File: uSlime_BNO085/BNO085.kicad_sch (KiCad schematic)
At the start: 12 parts, among them CN1 X1502WR-05K-N0SN, U5 BNO085

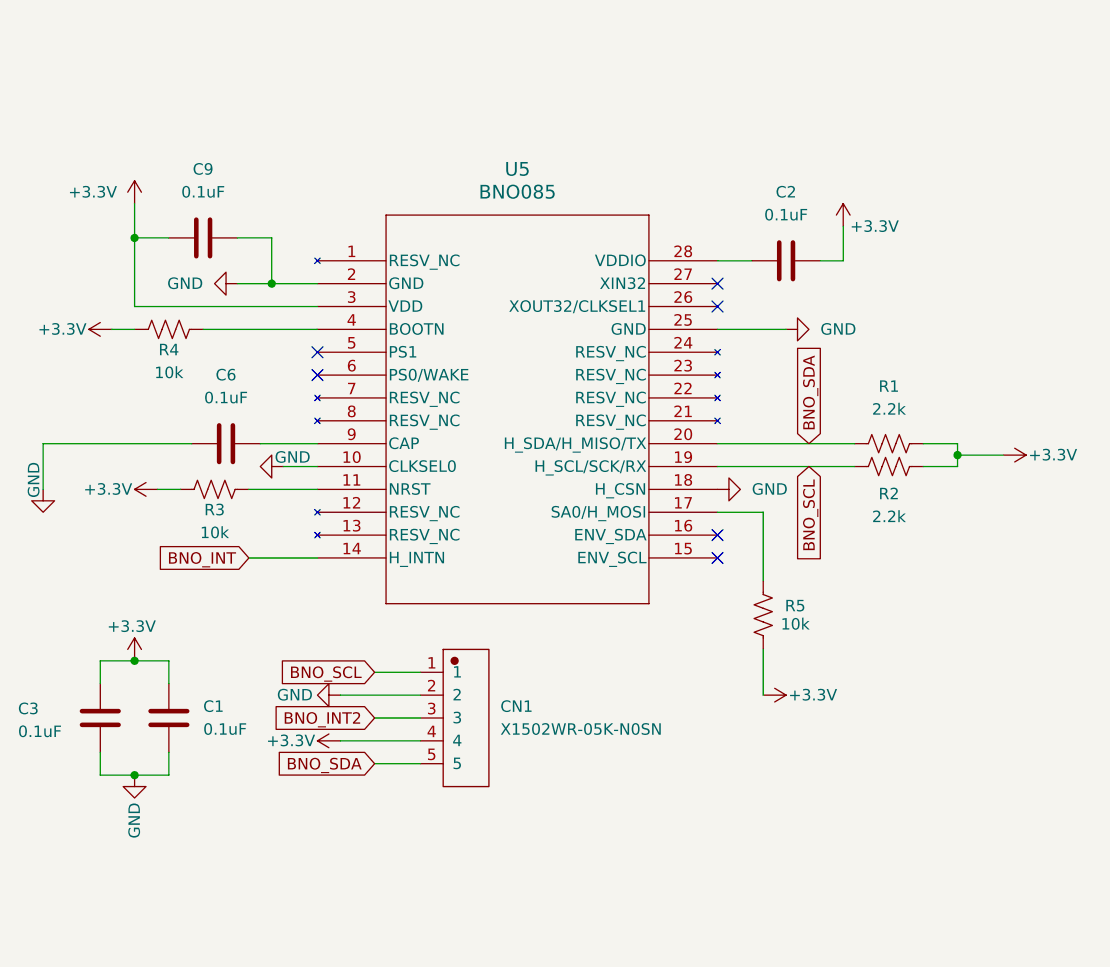
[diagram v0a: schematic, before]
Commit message: Faulty BNO085 footprint
First, I do not like you UltraLibrarian anymore, for you have wasted a
lot of time and effort (and money) on footprints that are just straight
up wrong. I am this close to unleashing unbridled rage on this but will
bottle it up for now.

Second, I took the BNO085 footprint from the official SlimeVR tracker
and put it in this project. At least they have the right footprint...

Stencils for the main microcontroller does not need to change but the
extension module got a revamp in favor of being more versatile. You can
now choose which I2C address the sensor operates on; just make sure you
bridge the right contacts.
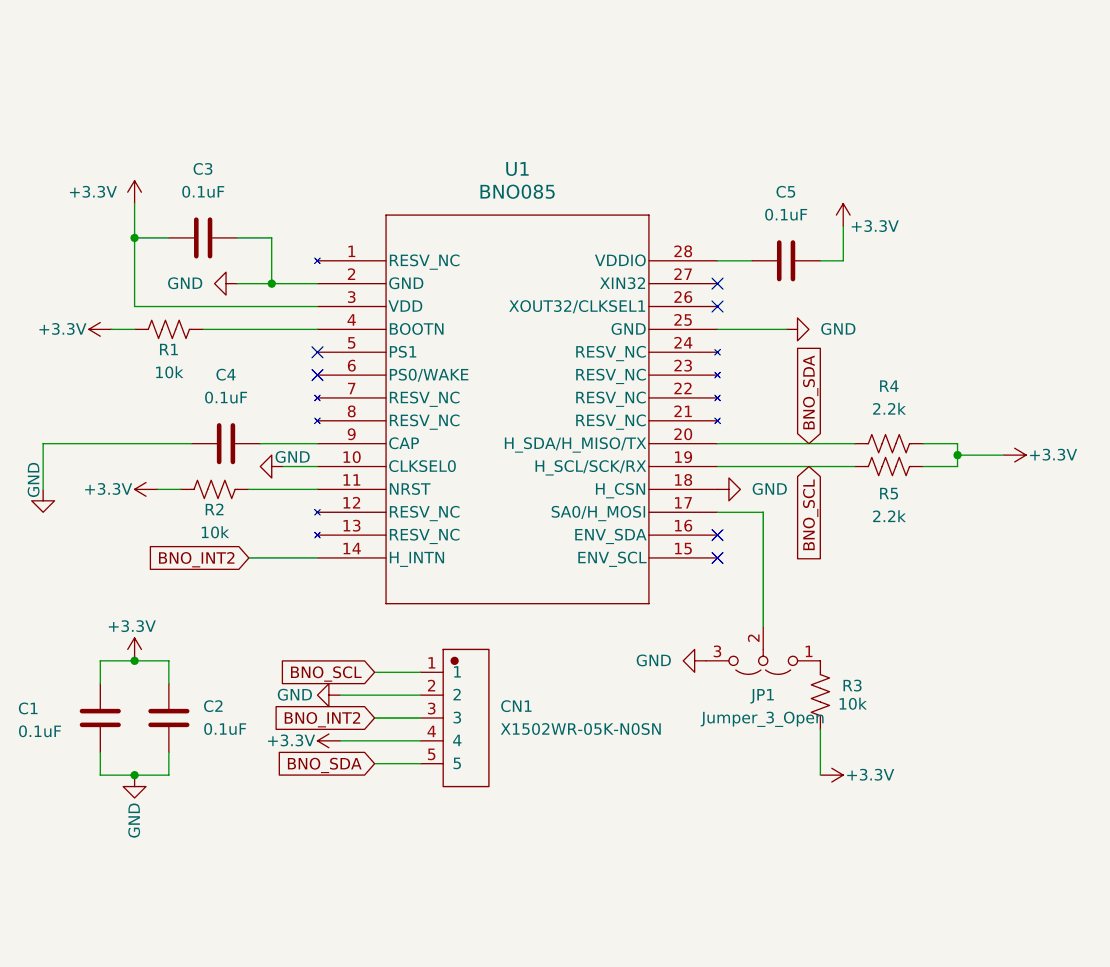
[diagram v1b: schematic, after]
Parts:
- removed R5: 10k, Resistor_SMD:R_0402_1005Metric, symbol uSlime:R_US
- added JP1: Jumper_3_Open, Jumper:SolderJumper-3_P1.3mm_Open_RoundedPad1.0x1.5mm, symbol uSlime:Jumper_3_Open
- added R3: 10k, Resistor_SMD:R_0402_1005Metric, symbol uSlime:R_US
- U1: renamed from U5; footprint uSlime-libs:LGA28_5.2X3.8_CEV -> uSlime-libs:BNO080
- renumbered C3 to C1, C1 to C2, C9 to C3, C6 to C4, C2 to C5, R4 to R1, R3 to R2, R1 to R4, R2 to R5
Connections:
- net BNO_INT is gone; now on net BNO_INT2: U1.14 (H_INTN)
- net +3.3V: now also R3.1
- net GND: now also JP1.3 (B)
- net at U1.17 (SA0/H_MOSI): now also JP1.2 (C)
- new net: JP1.1 (A), R3.2

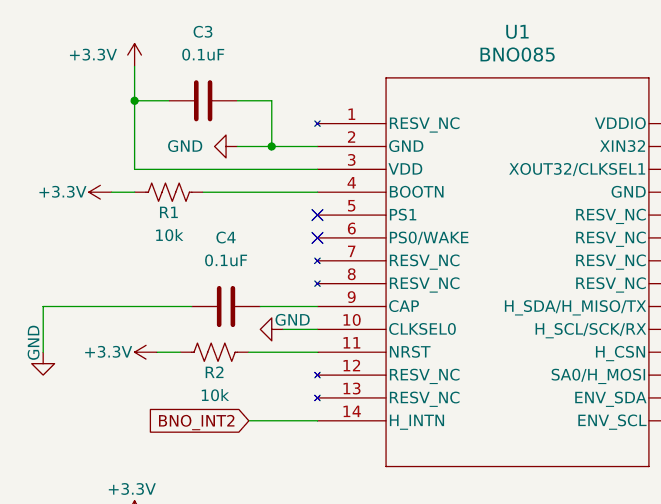
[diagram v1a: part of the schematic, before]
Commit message: update schmetic
fix pull up
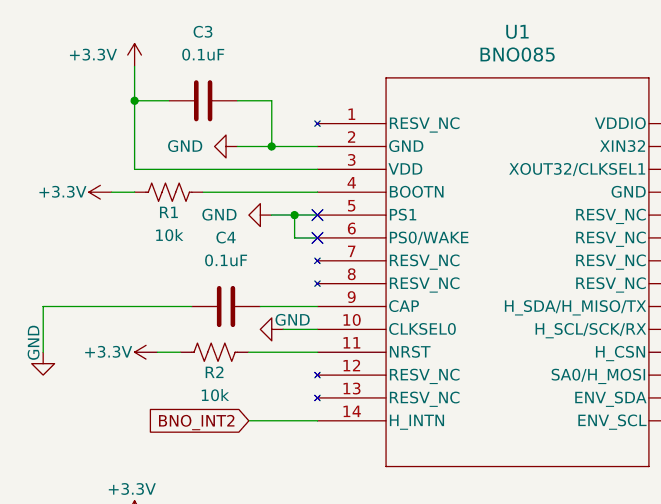
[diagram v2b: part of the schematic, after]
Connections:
- net GND: now also U1.5 (PS1), U1.6 (PS0/WAKE)
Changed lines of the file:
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@@
+	)
+	(junction
+		(at 113.03 87.63)
+		(diameter 0)
+		(color 0 0 0 0)
 	)
 	(junction
@@
 	(wire
 		(pts
+			(xy 113.03 90.17) (xy 115.57 90.17)
+		)
+		(stroke
+			(width 0)
+			(type default)
+		)
+	)
+	(wire
+		(pts
+			(xy 113.03 87.63) (xy 113.03 90.17)
+		)
+		(stroke
+			(width 0)
+			(type default)
+		)
+	)
+	(wire
+		(pts
 			(xy 110.49 74.93) (xy 110.49 80.01)
 		)
@@
 		(pts
 			(xy 163.83 77.47) (xy 160.02 77.47)
+		)
+		(stroke
+			(width 0)
+			(type default)
+		)
+	)
+	(wire
+		(pts
+			(xy 110.49 87.63) (xy 113.03 87.63)
+		)
+		(stroke
+			(width 0)
+			(type default)
+		)
+	)
+	(wire
+		(pts
+			(xy 113.03 87.63) (xy 115.57 87.63)
 		)
 		(stroke
@@
 					(unit 1)
 				)
+			)
+		)
+	)
+	(symbol
+		(lib_id "power:GND")
+		(at 110.49 87.63 270)
+		(unit 1)
+		(exclude_from_sim no)
+		(in_bom yes)
+		(on_board yes)
+		(dnp no)
+		(fields_autoplaced yes)
+		(property "Reference" "#PWR017"
+			(at 104.14 87.63 0)
+			(effects
+				(font
+					(size 1.27 1.27)
+				)
+				(hide yes)
+			)
+		)
+		(property "Value" "GND"
+			(at 106.68 87.6299 90)
+			(effects
+				(font
+					(size 1.27 1.27)
+				)
+				(justify right)
+			)
+		)
+		(property "Footprint" ""
+			(at 110.49 87.63 0)
+			(effects
+				(font
+					(size 1.27 1.27)
+				)
+				(hide yes)
+			)
+		)
+		(property "Datasheet" ""
+			(at 110.49 87.63 0)
+			(effects
+				(font
+					(size 1.27 1.27)
+				)
+				(hide yes)
+			)
+		)
+		(property "Description" "Power symbol creates a global label with name \"GND\" , ground"
+			(at 110.49 87.63 0)
+			(effects
+				(font
+					(size 1.27 1.27)
+				)
+				(hide yes)
+			)
+		)
+		(pin "1"
+		)
+		(instances
+			(project "uSlime_BNO085"
+				(path "/f32c1c49-f803-4e7c-a530-6db148a7ba36/1072de81-ddaf-4115-9b1e-8b480e2a0117"
+					(reference "#PWR017")
+					(unit 1)
+				)

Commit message: Update main PCB schematic
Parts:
- removed C5: 0.1uF, Capacitor_SMD:C_0402_1005Metric, symbol uSlime:C
- removed JP1: Jumper_3_Open, Jumper:SolderJumper-3_P1.3mm_Open_RoundedPad1.0x1.5mm, symbol uSlime:Jumper_3_Open
- removed R5: 2.2k, Resistor_SMD:R_0402_1005Metric, symbol uSlime:R_US
- R3: value 10k -> 2.2k
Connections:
- net +3.3V: now also CN1.2, R2.2, R4.1, U1.28 (VDDIO); no longer CN1.4, R2.1, R4.2
- net BNO_INT2: no longer U1.14 (H_INTN)
- net BNO_SCL: now also CN1.5, R4.2; no longer CN1.1
- net BNO_SDA: now also CN1.1, R3.2; no longer CN1.5, R4.1
- net GND: now also CN1.4; no longer CN1.2
- net at U1.11 (NRST): now also R2.1; no longer R2.2
- new net BNO_INT: U1.14 (H_INTN)
- no-connect marks 6 -> 5
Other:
- moved on the sheet: C1, C2

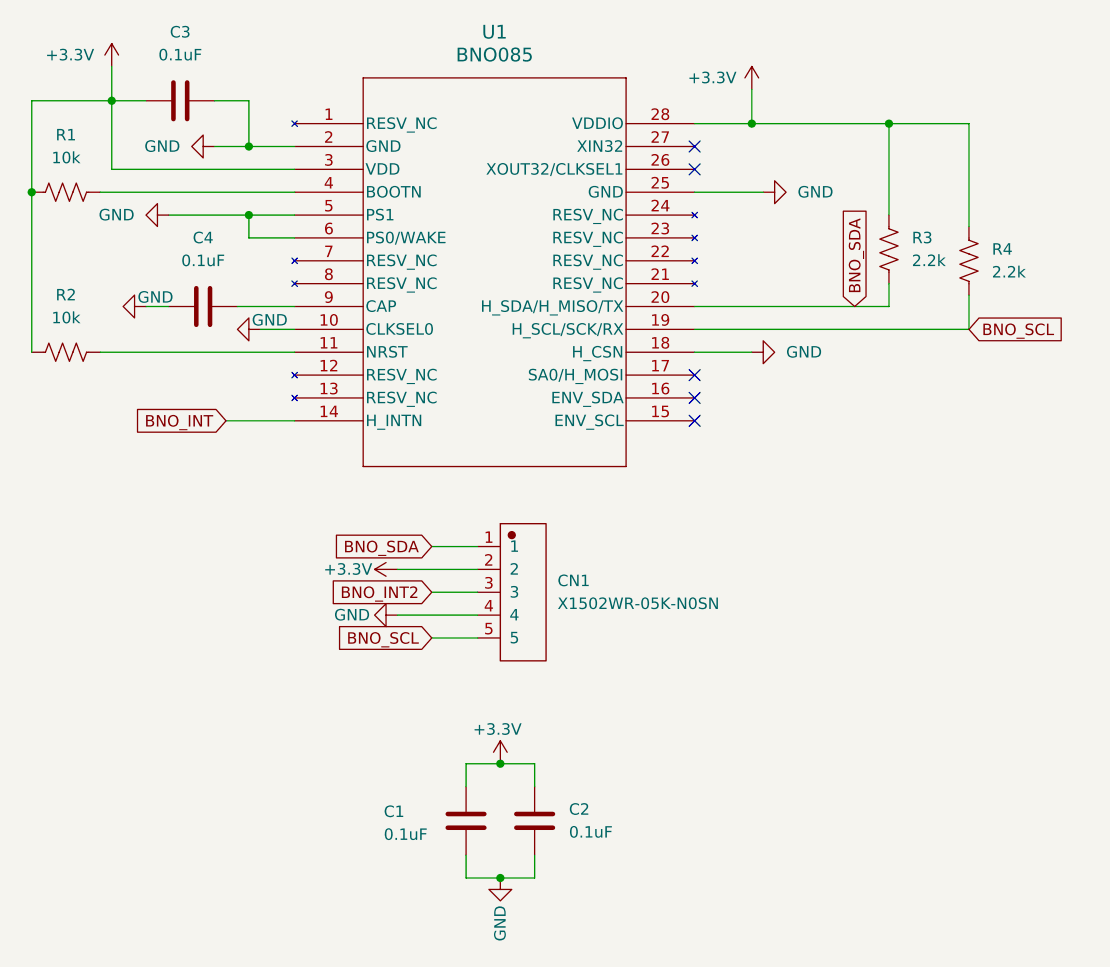
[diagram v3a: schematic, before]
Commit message: v0.0.2a Modify BNO I2C
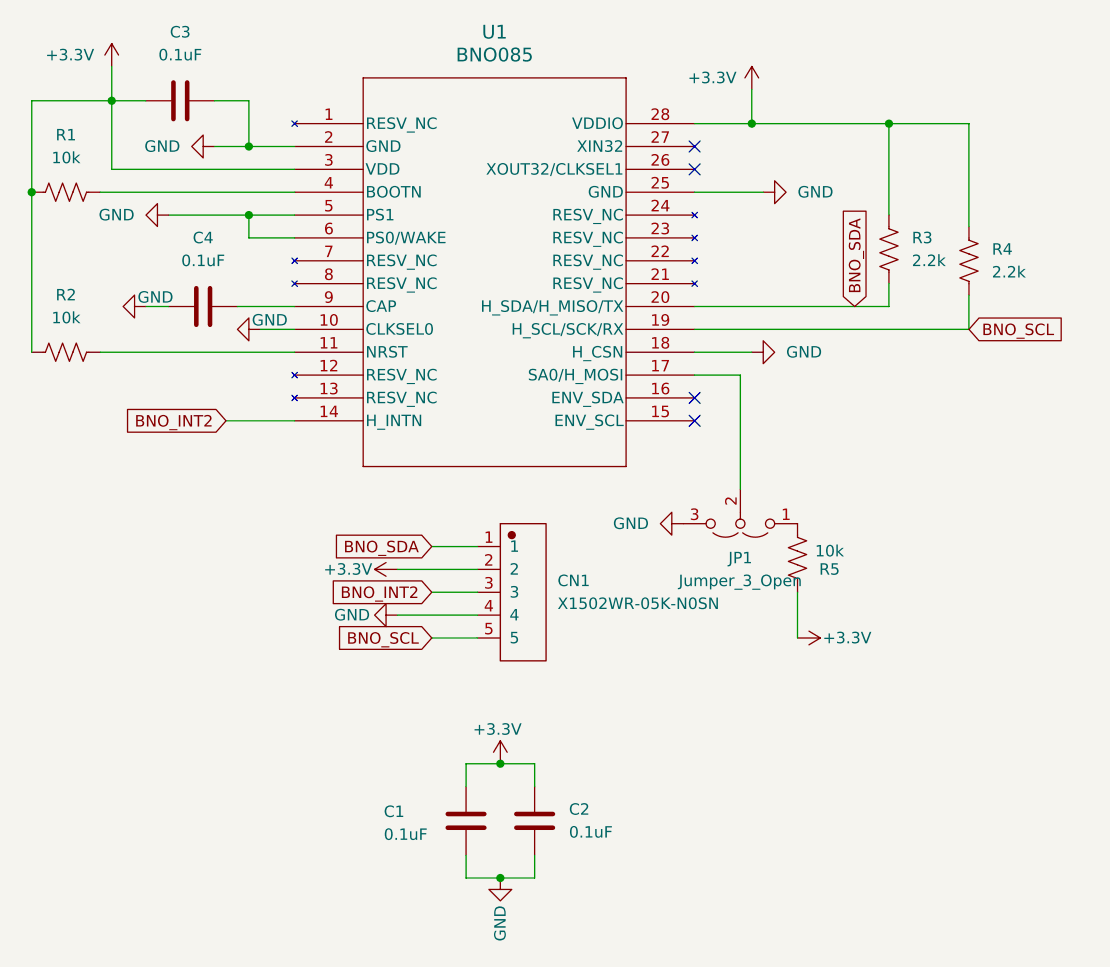
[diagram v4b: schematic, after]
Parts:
- added JP1: Jumper_3_Open, Jumper:SolderJumper-3_P1.3mm_Open_RoundedPad1.0x1.5mm, symbol uSlime:Jumper_3_Open
- added R5: 10k, Resistor_SMD:R_0402_1005Metric, symbol uSlime:R_US
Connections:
- net BNO_INT is gone; now on net BNO_INT2: U1.14 (H_INTN)
- net +3.3V: now also R5.2
- net GND: now also JP1.3 (B)
- net at U1.17 (SA0/H_MOSI): now also JP1.2 (C)
- new net: JP1.1 (A), R5.1
- no-connect marks 5 -> 4

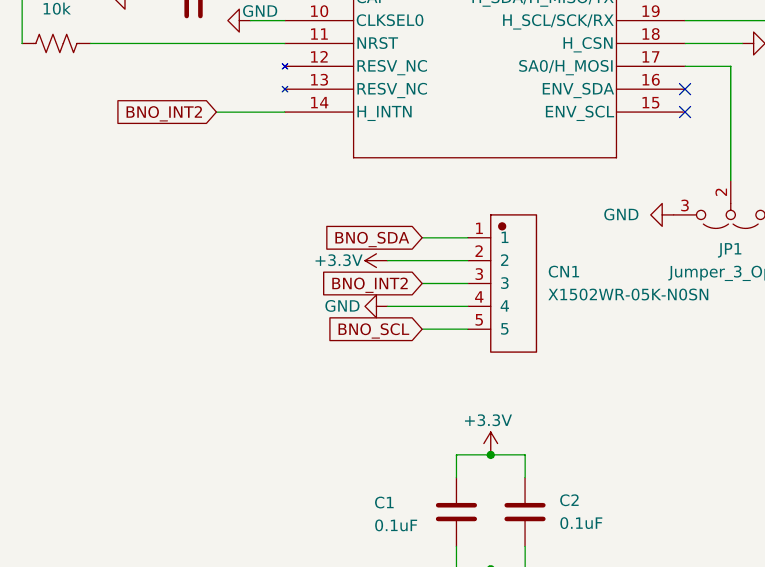
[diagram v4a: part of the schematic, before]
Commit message: Fix BNO wrong pin order
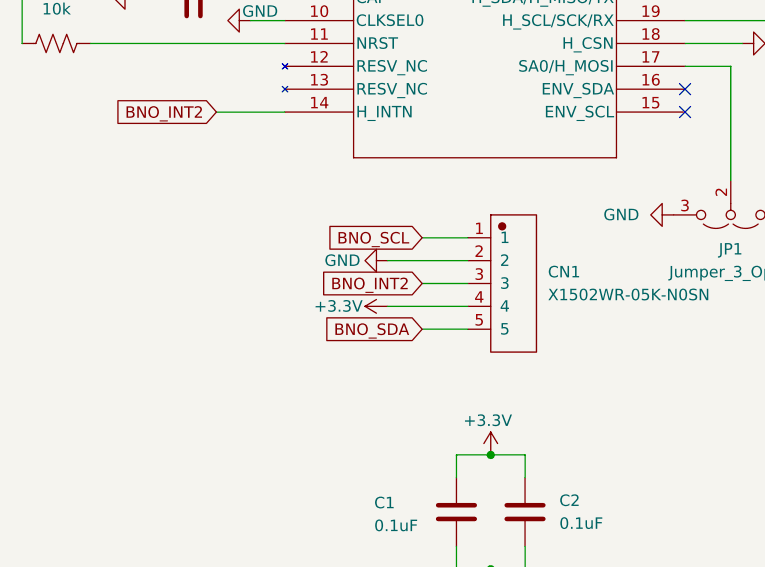
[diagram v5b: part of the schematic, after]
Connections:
- net +3.3V: now also CN1.4; no longer CN1.2
- net BNO_SCL: now also CN1.1; no longer CN1.5
- net BNO_SDA: now also CN1.5; no longer CN1.1
- net GND: now also CN1.2; no longer CN1.4
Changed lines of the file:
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@@
-		)
-	)
-	(global_label "BNO_SCL"
-		(shape input)
-		(at 128.27 119.38 180)
-		(fields_autoplaced yes)
-		(effects
-			(font
-				(size 1.27 1.27)
-			)
-			(justify right)
-		)
-		(property "Intersheetrefs" "${INTERSHEET_REFS}"
-			(at 116.8786 119.38 0)
-			(effects
-				(font
-					(size 1.27 1.27)
-				)
-				(justify right)
-				(hide yes)
-			)
 		)
 	)
@@
 	(global_label "BNO_SDA"
 		(shape input)
+		(at 128.27 119.38 180)
+		(fields_autoplaced yes)
+		(effects
+			(font
+				(size 1.27 1.27)
+			)
+			(justify right)
+		)
+		(property "Intersheetrefs" "${INTERSHEET_REFS}"
+			(at 116.8181 119.38 0)
+			(effects
+				(font
+					(size 1.27 1.27)
+				)
+				(justify right)
+				(hide yes)
+			)
+		)
+	)
+	(global_label "BNO_SDA"
+		(shape input)
 		(at 175.26 82.55 90)
 		(fields_autoplaced yes)
@@
 		)
 	)
-	(global_label "BNO_SDA"
+	(global_label "BNO_SCL"
 		(shape input)
 		(at 128.27 109.22 180)
@@
 		)
 		(property "Intersheetrefs" "${INTERSHEET_REFS}"
-			(at 116.8181 109.22 0)
+			(at 116.8786 109.22 0)
 			(effects
 				(font
@@
 	)
 	(symbol
+		(lib_id "power:+3.3V")
+		(at 124.46 116.84 90)
+		(unit 1)
+		(exclude_from_sim no)
+		(in_bom yes)
+		(on_board yes)
+		(dnp no)
+		(property "Reference" "#PWR08"
+			(at 128.27 116.84 0)
+			(effects
+				(font
+					(size 1.27 1.27)
+				)
+				(hide yes)
+			)
+		)
+		(property "Value" "+3.3V"
+			(at 121.666 116.84 90)
+			(effects
+				(font
+					(size 1.27 1.27)
+				)
+				(justify left)
+			)
+		)
+		(property "Footprint" ""
+			(at 124.46 116.84 0)
+			(effects
+				(font
+					(size 1.27 1.27)
+				)
+				(hide yes)
+			)
+		)
+		(property "Datasheet" ""
+			(at 124.46 116.84 0)
+			(effects
+				(font
+					(size 1.27 1.27)
+				)
+				(hide yes)
+			)
+		)
+		(property "Description" "Power symbol creates a global label with name \"+3.3V\""
+			(at 124.46 116.84 0)
+			(effects
+				(font
+					(size 1.27 1.27)
+				)
+				(hide yes)
+			)
+		)
+		(pin "1"
+		)
+		(instances
+			(project "uSlime_BNO085"
+				(path "/f32c1c49-f803-4e7c-a530-6db148a7ba36/1072de81-ddaf-4115-9b1e-8b480e2a0117"
+					(reference "#PWR08")
+					(unit 1)
+				)
+			)
+		)
+	)
+	(symbol
 		(lib_id "power:GND")
 		(at 156.21 106.68 270)
@@
 	(symbol
 		(lib_id "power:GND")
-		(at 124.46 116.84 270)
-		(unit 1)
-		(exclude_from_sim no)
-		(in_bom yes)
-		(on_board yes)
-		(dnp no)
-		(property "Reference" "#PWR09"
-			(at 118.11 116.84 0)
-			(effects
-				(font
-					(size 1.27 1.27)
-				)
-				(hide yes)
-			)
-		)
-		(property "Value" "GND"
-			(at 121.412 116.84 90)
-			(effects
-				(font
-					(size 1.27 1.27)
-				)
-				(justify right)
-			)
-		)
-		(property "Footprint" ""
-			(at 124.46 116.84 0)
-			(effects
-				(font
-					(size 1.27 1.27)
-				)
-				(hide yes)
-			)
-		)
-		(property "Datasheet" ""
-			(at 124.46 116.84 0)
-			(effects
-				(font
-					(size 1.27 1.27)
-				)
-				(hide yes)
-			)
-		)
-		(property "Description" "Power symbol creates a global label with name \"GND\" , ground"
-			(at 124.46 116.84 0)
-			(effects
-				(font
-					(size 1.27 1.27)
-				)
-				(hide yes)
-			)
-		)
-		(pin "1"
-		)
-		(instances
-			(project "uSlime_BNO085"
-				(path "/f32c1c49-f803-4e7c-a530-6db148a7ba36/1072de81-ddaf-4115-9b1e-8b480e2a0117"
-					(reference "#PWR09")
-					(unit 1)
-				)
-			)
-		)
-	)
-	(symbol
-		(lib_id "power:GND")
 		(at 165.1 69.85 90)
 		(unit 1)
@@
 	)
 	(symbol
-		(lib_id "power:+3.3V")
-		(at 124.46 111.76 90)
-		(unit 1)
-		(exclude_from_sim no)
-		(in_bom yes)
-		(on_board yes)
-		(dnp no)
-		(property "Reference" "#PWR08"
-			(at 128.27 111.76 0)
-			(effects
-				(font
-					(size 1.27 1.27)
-				)
-				(hide yes)
-			)
-		)
-		(property "Value" "+3.3V"
-			(at 121.666 111.76 90)
-			(effects
-				(font
-					(size 1.27 1.27)
-				)
-				(justify left)
+		(lib_id "power:GND")
+		(at 124.46 111.76 270)
+		(unit 1)
+		(exclude_from_sim no)
+		(in_bom yes)
+		(on_board yes)
+		(dnp no)
+		(property "Reference" "#PWR09"
+			(at 118.11 111.76 0)
+			(effects
+				(font
+					(size 1.27 1.27)
+				)
+				(hide yes)
+			)
+		)
+		(property "Value" "GND"
+			(at 121.412 111.76 90)
+			(effects
+				(font
+					(size 1.27 1.27)
+				)
+				(justify right)
 			)
 		)
@@
 			)
 		)
-		(property "Description" "Power symbol creates a global label with name \"+3.3V\""
+		(property "Description" "Power symbol creates a global label with name \"GND\" , ground"
 			(at 124.46 111.76 0)
 			(effects
@@
 			(project "uSlime_BNO085"
 				(path "/f32c1c49-f803-4e7c-a530-6db148a7ba36/1072de81-ddaf-4115-9b1e-8b480e2a0117"
-					(reference "#PWR08")
-					(unit 1)
-				)
+					(reference "#PWR09")
+					(unit 1)
+				)
